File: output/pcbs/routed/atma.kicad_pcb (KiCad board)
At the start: 2 copper layers, 114.1 x 85.7 mm, 23 parts

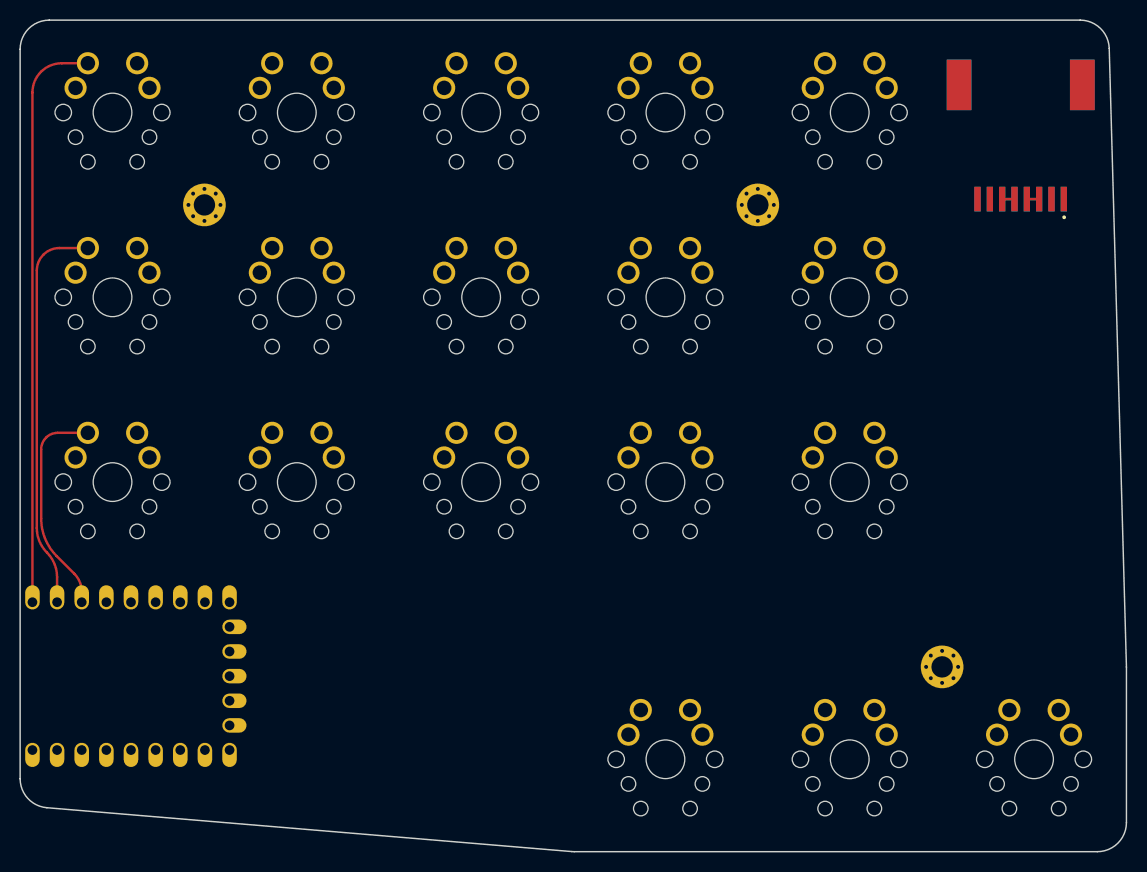
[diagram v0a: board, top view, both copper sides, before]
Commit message: small outline tweak
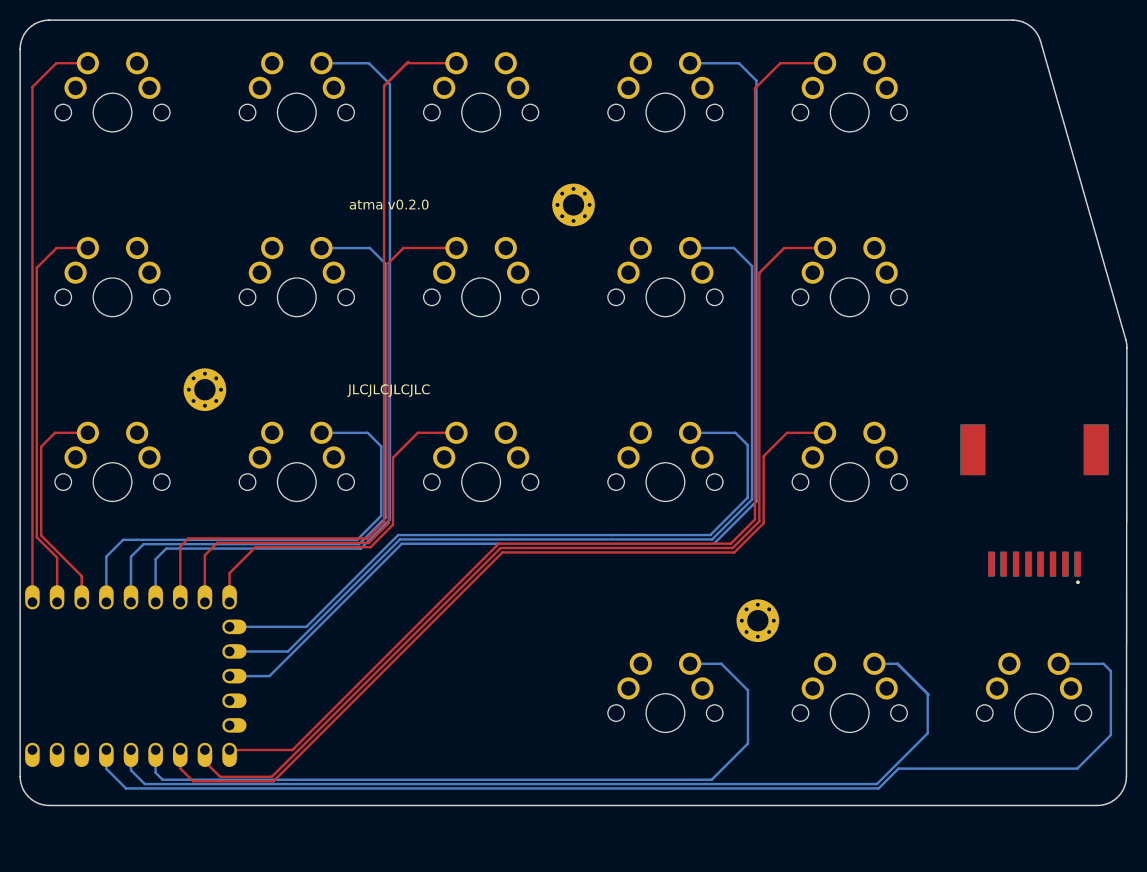
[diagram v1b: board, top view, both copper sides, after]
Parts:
- moved ? 37.7 mm to (247.4, 160.0)
- moved _5 19.6 mm to (218.9, 166.7)
- moved _3 19.1 mm to (161.9, 142.9)
- moved _4 19.0 mm to (199.9, 123.8)
- moved S16 4.76 mm to (209.4, 176.2)
- moved S17 4.76 mm to (228.4, 176.2)
- moved S18 4.76 mm to (247.4, 176.2)
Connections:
- ? pad 10: matrix_index_top -> matrix_index_bottom
- ? pad 12: matrix_index_bottom -> matrix_index_top
- ? pad 15: matrix_inner_bottom -> matrix_inner_top
- ? pad 17: matrix_inner_top -> matrix_inner_bottom
- ? pad 3: GP12 -> GP13
- ? pad 4: GP12 -> GP13
- ? pad 5: GP13 -> GP12
- ? pad 6: GP13 -> GP12
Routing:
- net thumbfan_far_home: track 0.00 -> 120.9 mm
- net matrix_inner_top: track 0.00 -> 116.7 mm
- net matrix_index_top: track 0.00 -> 112.7 mm
- net matrix_inner_home: track 0.00 -> 103.4 mm
- net thumbfan_home_home: track 0.00 -> 102.4 mm
- net matrix_index_home: track 0.00 -> 91.6 mm
- net matrix_inner_bottom: track 0.00 -> 87.8 mm
- net matrix_middle_top: track 0.00 -> 84.7 mm
- net matrix_ring_top: track 0.00 -> 83.1 mm
- net thumbfan_near_home: track 0.00 -> 77.8 mm
- net matrix_index_bottom: track 0.00 -> 70.8 mm
- net matrix_ring_home: track 0.00 -> 66.1 mm
- net matrix_middle_home: track 0.00 -> 59.6 mm
- net matrix_ring_bottom: track 0.00 -> 48.7 mm
- net matrix_middle_bottom: track 0.00 -> 36.4 mm
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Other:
- board size 114.1 x 85.7 mm -> 114.1 x 81 mm
- board text added: "JLCJLCJLCJLC"
- board text added: "atma v0.2.0"
